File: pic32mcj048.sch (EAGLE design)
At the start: 1 part

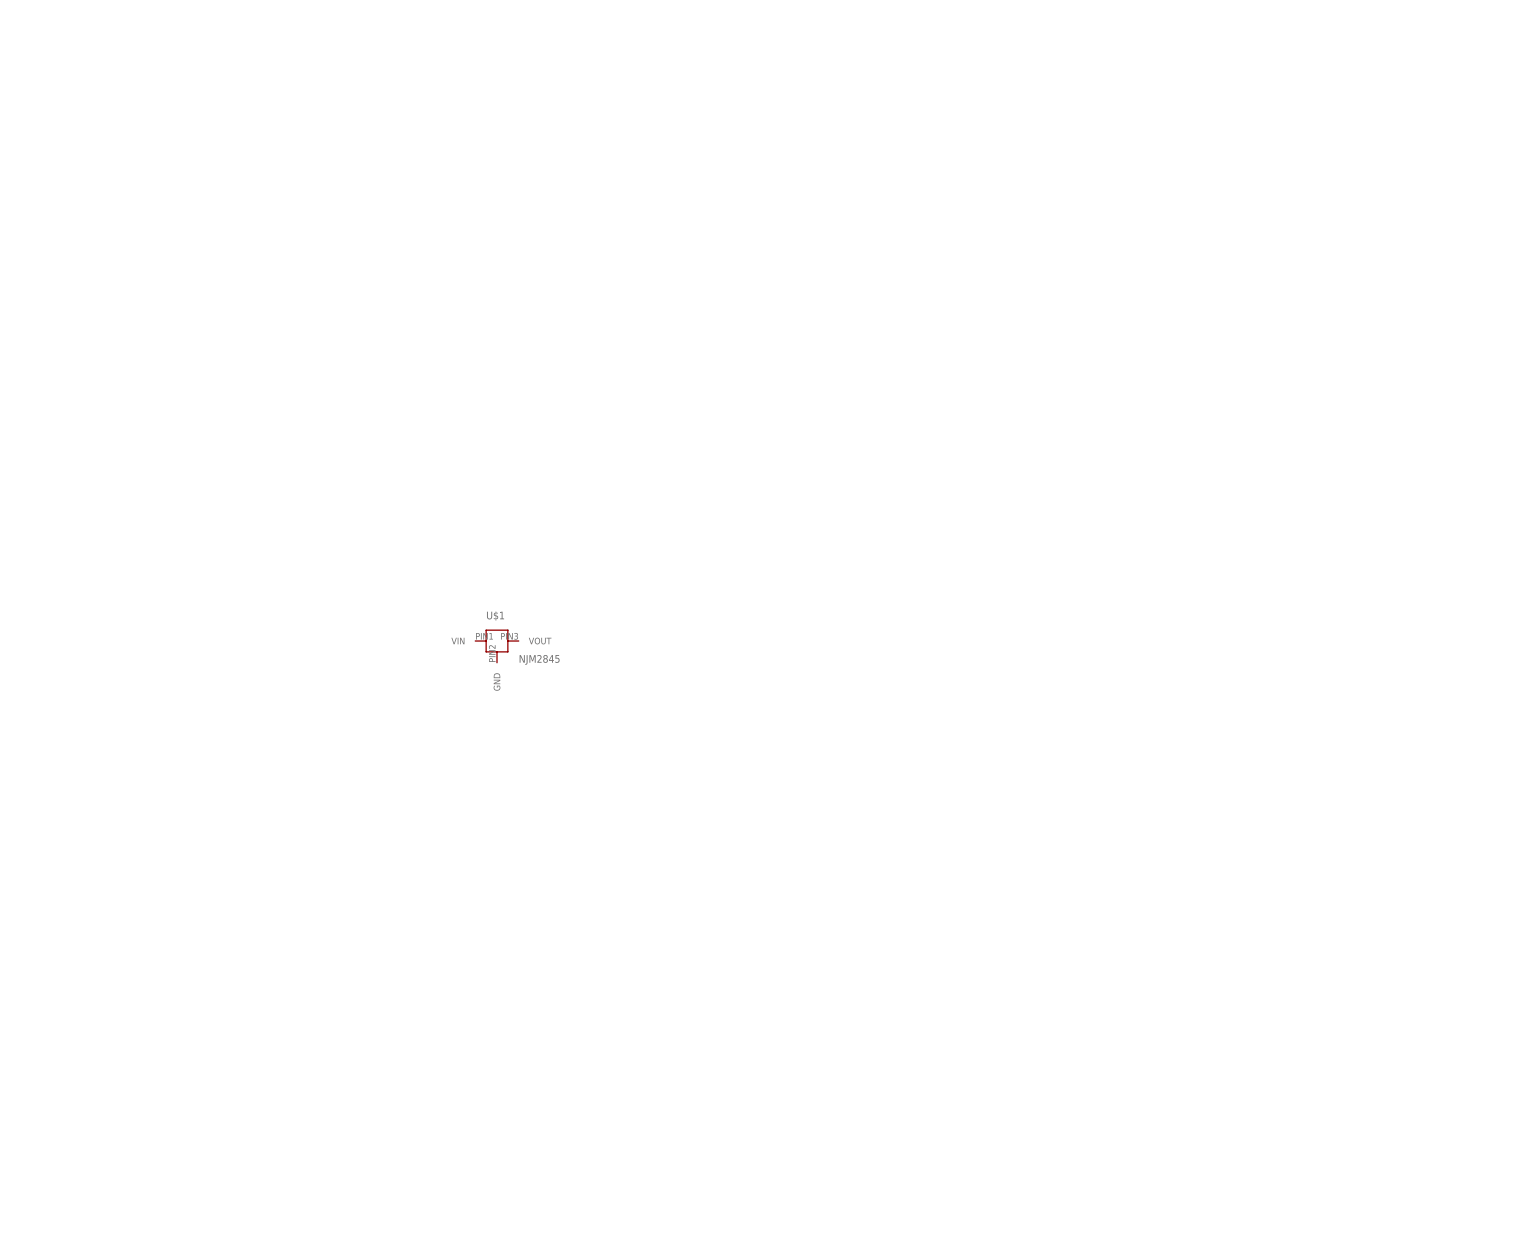
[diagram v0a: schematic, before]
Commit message: リセット回路、書き込み回路を作った
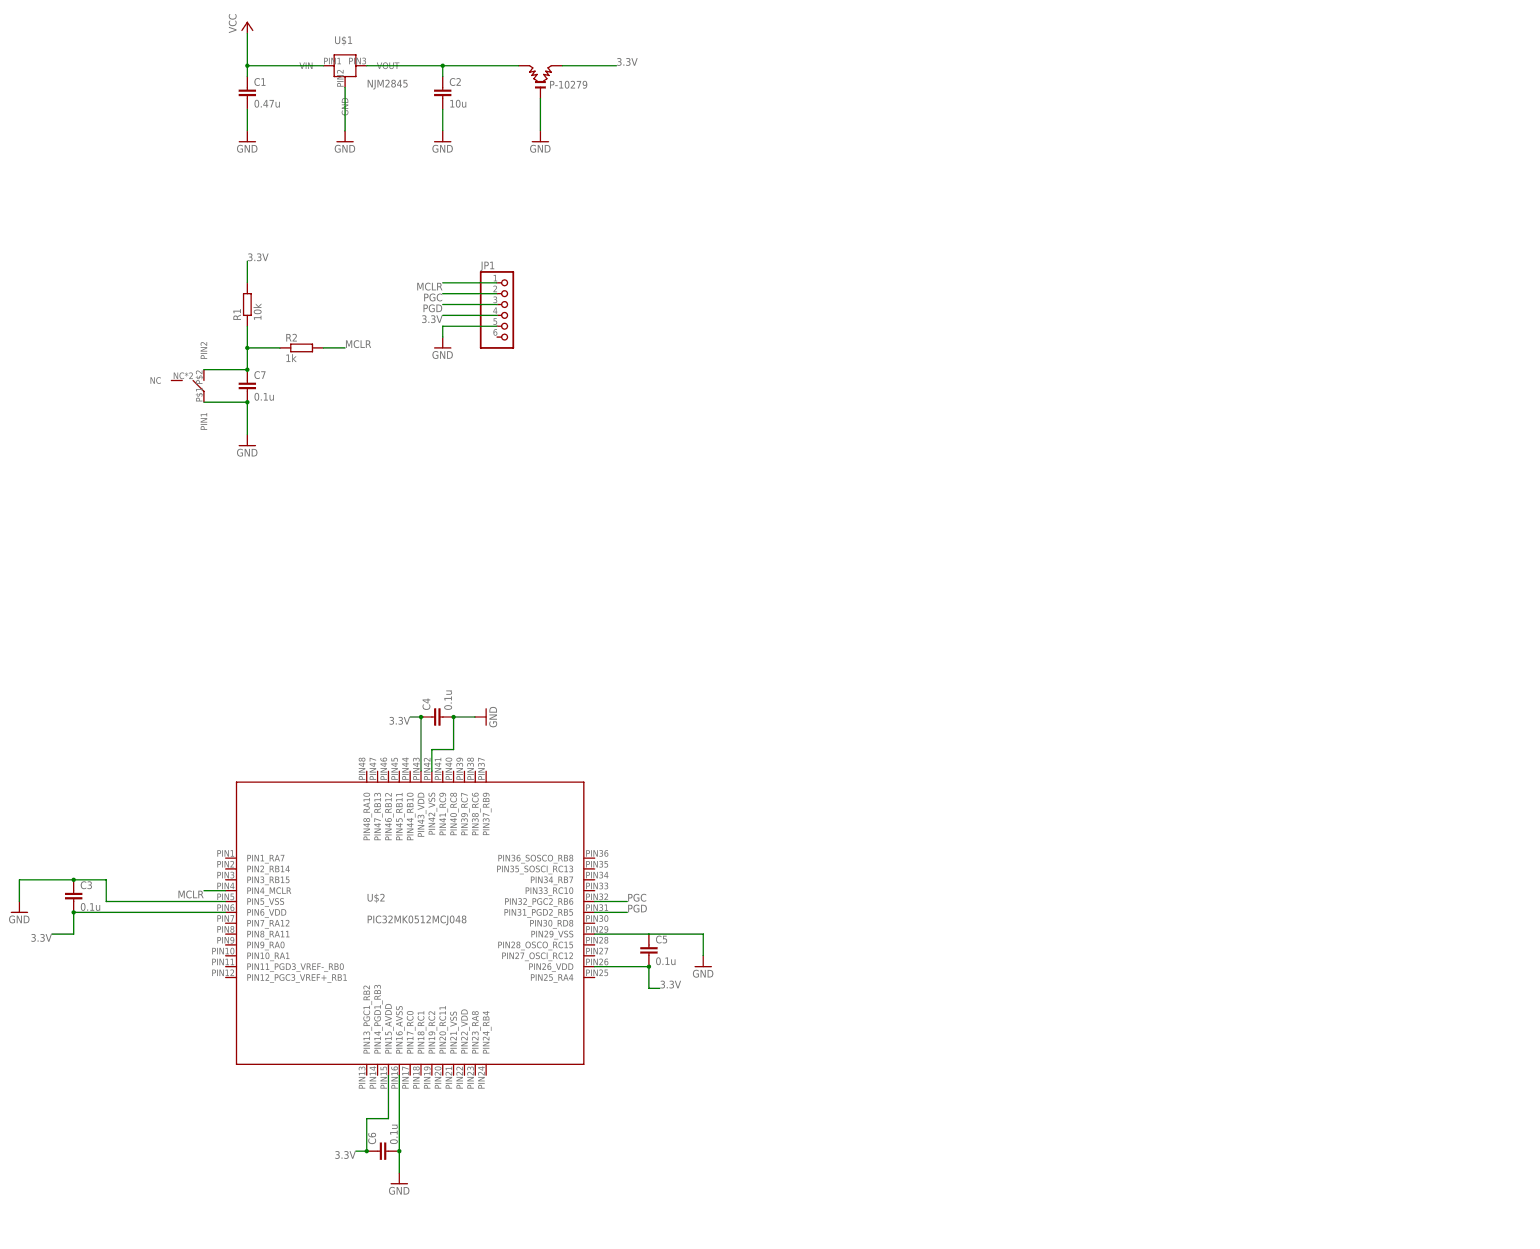
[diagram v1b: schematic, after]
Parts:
- added C1: 0.47u, rcl:C-EUC1608
- added C2: 10u, rcl:C-EUC1608
- added C3, C4, C5, C6, C7: 0.1u, rcl:C-EUC1608
- added JP1: (no value), pinhead:PINHD-1X6
- added P-10279: (no value), user_emifilter:LCL
- added R1: 10k, user_rcl:R_REG
- added R2: 1k, user_rcl:R_REG
- added U$2: PIC32MK0512MCJ048, user_ic:PIC32MK0512MCJ048
- added U$3: TAKUTOSUITTI2, user_swich:TAKUTOSUITTI2
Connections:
- new net 3.3V: C3.2, C4.1, C5.2, C6.1, JP1.4, P-10279.2, R1.2, U$2.PIN15_AVDD, U$2.PIN26_VDD, U$2.PIN43_VDD, U$2.PIN6_VDD
- new net GND: C1.2, C2.2, C3.1, C4.2, C5.1, C6.2, C7.2, JP1.5, P-10279.GND, U$1.GND, U$2.PIN16_AVSS, U$2.PIN29_VSS, U$2.PIN42_VSS, U$2.PIN5_VSS, U$3.PIN1
- new net MCLR: JP1.1, R2.2, U$2.PIN4_MCLR
- new net N$1: C2.1, P-10279.1, U$1.VOUT
- new net N$2: C7.1, R1.1, R2.1, U$3.PIN2
- new net PGC: JP1.2, U$2.PIN32_PGC2_RB6
- new net PGD: JP1.3, U$2.PIN31_PGD2_RB5
- new net VCC: C1.1, U$1.VIN
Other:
- moved on the sheet: U$1

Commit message: brdfileを編集
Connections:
- net 3.3V: now also JP1.2; no longer JP1.4
- net GND: now also JP1.3; no longer JP1.5
- net PGC: now also JP1.5; no longer JP1.2
- net PGD: now also JP1.4; no longer JP1.3
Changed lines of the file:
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@@
 <part name="R2" library="user_rcl" deviceset="R_REG" device="" value="1k"/>
 <part name="JP1" library="pinhead" library_urn="urn:adsk.eagle:library:325" deviceset="PINHD-1X6" device="" package3d_urn="urn:adsk.eagle:package:22472/2"/>
-<part name="GND10" library="supply1" library_urn="urn:adsk.eagle:library:371" deviceset="GND" device=""/>
 <part name="U$3" library="user_swich" deviceset="TAKUTOSUITTI2" device=""/>
 </parts>
@@
 <attribute name="VALUE" x="16.51" y="132.08" size="1.778" layer="96"/>
 </instance>
-<instance part="GND10" gate="1" x="7.62" y="134.62" smashed="yes">
-<attribute name="VALUE" x="5.08" y="132.08" size="1.778" layer="96"/>
-</instance>
 <instance part="U$3" gate="G$1" x="-50.8" y="124.46" smashed="yes" rot="R90"/>
 </instances>
@@
 </segment>
 <segment>
-<pinref part="JP1" gate="A" pin="4"/>
-<wire x1="20.32" y1="142.24" x2="7.62" y2="142.24" width="0.1524" layer="91"/>
-<label x="7.62" y="142.24" size="1.778" layer="95" rot="R180"/>
+<pinref part="JP1" gate="A" pin="2"/>
+<wire x1="20.32" y1="147.32" x2="7.62" y2="147.32" width="0.1524" layer="91"/>
+<label x="7.62" y="147.32" size="1.778" layer="95"/>
 </segment>
 </net>
@@
 </segment>
 <segment>
-<pinref part="JP1" gate="A" pin="5"/>
-<wire x1="20.32" y1="139.7" x2="7.62" y2="139.7" width="0.1524" layer="91"/>
-<pinref part="GND10" gate="1" pin="GND"/>
-<wire x1="7.62" y1="139.7" x2="7.62" y2="137.16" width="0.1524" layer="91"/>
+<pinref part="JP1" gate="A" pin="3"/>
+<wire x1="20.32" y1="144.78" x2="7.62" y2="144.78" width="0.1524" layer="91"/>
+<label x="7.62" y="144.78" size="1.778" layer="95"/>
 </segment>
 </net>
@@
 <pinref part="JP1" gate="A" pin="1"/>
 <wire x1="20.32" y1="149.86" x2="7.62" y2="149.86" width="0.1524" layer="91"/>
-<label x="7.62" y="149.86" size="1.778" layer="95" rot="R180"/>
+<label x="7.62" y="149.86" size="1.778" layer="95"/>
 </segment>
 </net>
@@
 </segment>
 <segment>
-<pinref part="JP1" gate="A" pin="2"/>
-<wire x1="20.32" y1="147.32" x2="7.62" y2="147.32" width="0.1524" layer="91"/>
-<label x="7.62" y="147.32" size="1.778" layer="95" rot="R180"/>
+<pinref part="JP1" gate="A" pin="5"/>
+<wire x1="20.32" y1="139.7" x2="7.62" y2="139.7" width="0.1524" layer="91"/>
+<label x="7.62" y="139.7" size="1.778" layer="95"/>
 </segment>
 </net>
@@
 </segment>
 <segment>
-<pinref part="JP1" gate="A" pin="3"/>
-<wire x1="20.32" y1="144.78" x2="7.62" y2="144.78" width="0.1524" layer="91"/>
-<label x="7.62" y="144.78" size="1.778" layer="95" rot="R180"/>
-</segment>
-</net>
+<pinref part="JP1" gate="A" pin="4"/>
+<wire x1="20.32" y1="142.24" x2="7.62" y2="142.24" width="0.1524" layer="91"/>
+<label x="7.62" y="142.24" size="1.778" layer="95"/>
+</segment>
+</net>

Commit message: sch完成
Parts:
- added C10, C11: 22p, rcl:C-EUC1608
- added C8: 0.1u, rcl:C-EUC1608
- added C9: 10u, rcl:C-EUC1608
- added IC1: (no value), user_ic:MCP2562
- added JP2, JP3: (no value), pinhead:PINHD-1X15
- added OSC1: 16M, user_osc:CSTN#
- added R3, R4, R5, R6: 10k, user_rcl:R_REG
- added R7: 1k, user_rcl:R_REG
- added R8: (no value), user_rcl:R_REG
- added R_I1: 4.7k, user_rcl:R_SHUGOU2
- added U$5: RGB_LED, user_leds:RGB_LED
- added U$6: FDC6305, user_tr_fet_igbt:FDC6305
- added U$7: NJM2380, user_ic:NJM2380
- added X1: 32.768k, user_osc:FC255
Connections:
- new net C1RX: IC1.RXD, U$2.PIN25_RA4
- new net C1TX: IC1.TXD, U$2.PIN34_RB7
- new net CANH: IC1.CANH, JP3.9
- new net CANL: IC1.CANL, JP3.10
- new net LED_G: U$2.PIN33_RC10, U$6.PIN1_G1
- new net LED_R: U$2.PIN30_RD8, U$6.PIN3_G2
- new net N$11: R8.1, U$2.PIN36_SOSCO_RB8
- new net N$13: R4.1, U$5.B_A
- new net N$14: R5.1, U$5.G_A
- new net N$15: R6.1, U$5.R_A
- new net N$21: R_I1.7, R_I1.8, U$7.PIN5_REF
- new net N$3: OSC1.IN, U$2.PIN28_OSCO_RC15
- new net N$4: OSC1.OUT, U$2.PIN27_OSCI_RC12
- new net N$45: R_I1.2, R_I1.3
- new net N$46: R_I1.5, R_I1.6
- new net N$5: IC1.STBY, R3.1
- new net N$6: C10.1, R8.2, X1.2
- new net N$7: C11.1, U$2.PIN35_SOSCI_RC13, X1.1
- new net N$8: U$5.G_K, U$6.PIN6_D1
- new net N$9: U$5.R_K, U$6.PIN4_D2
- new net RA0: U$2.PIN9_RA0
- new net RA1: U$2.PIN10_RA1
- new net RA10: JP2.10, U$2.PIN48_RA10
- new net RA11: U$2.PIN8_RA11
- new net RA12: U$2.PIN7_RA12
- new net RA7: U$2.PIN1_RA7
- new net RA8: JP3.2, U$2.PIN23_RA8
- new net RB10: JP2.6, U$2.PIN44_RB10
- new net RB11: JP2.7, U$2.PIN45_RB11
- new net RB12: JP2.8, U$2.PIN46_RB12
- new net RB13: JP2.9, U$2.PIN47_RB13
- new net RB14: U$2.PIN2_RB14
- new net RB15: U$2.PIN3_RB15
- new net RB2: JP3.8, U$2.PIN13_PGC1_RB2
- new net RB3: JP3.7, U$2.PIN14_PGD1_RB3
- new net RB4: JP3.1, U$2.PIN24_RB4
- new net RB9: JP2.1, U$2.PIN37_RB9
- new net RC0: JP3.6, U$2.PIN17_RC0
- new net RC1: JP3.5, U$2.PIN18_RC1
- new net RC11: JP3.3, U$2.PIN20_RC11
- new net RC2: JP3.4, U$2.PIN19_RC2
- new net RC6: JP2.2, U$2.PIN38_RC6
- new net RC7: JP2.3, U$2.PIN39_RC7
- new net RC8: JP2.4, U$2.PIN40_RC8
- new net RC9: JP2.5, U$2.PIN41_RC9
- new net VREF+: C9.1, R7.1, R_I1.1, U$2.PIN12_PGC3_VREF+_RB1, U$7.PIN4_C
- net 3.3V: now also C8.2, IC1.VIO, JP2.11, JP3.11, R4.2, R5.2, R6.2, U$2.PIN22_VDD
- net GND: now also C10.2, C11.2, C8.1, C9.2, IC1.VSS, JP2.12, JP2.14, JP3.12, JP3.14, OSC1.GND, R_I1.4, U$2.PIN11_PGD3_VREF-_RB0, U$2.PIN21_VSS, U$5.B_K, U$6.PIN2_S2, U$6.PIN5_S1, U$7.PIN2_A
- net VCC: now also IC1.VDD, JP2.13, JP2.15, JP3.13, JP3.15, R3.2, R7.2
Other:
- moved on the sheet: C1, C2, C3, C4, C5, C6, C7, JP1, P-10279, R1, R2, U$1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

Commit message: 基本設計完了、あとは調整など
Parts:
- added C12, C13: 0.1u, rcl:C-EUC1608
- added C14: 0.47u, rcl:C-EUC1608
- added R9: 120, user_rcl:R_REG
- added U$4: XH_2P, user_conector:XH_2P
- added U$8: NJM2391, user_ic:NJM2391
- R4, R5, R6: value 10k -> 1k
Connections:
- removed net CANH: IC1.CANH, JP3.9
- removed net CANL: IC1.CANL, JP3.10
- new net +5V: C1.1, C12.1, C13.1, IC1.VDD, JP3.15, R3.2, R7.2, U$1.VIN, U$8.VOUT
- new net CAN_N: IC1.CANL, JP3.1, R9.1
- new net CAN_P: IC1.CANH, JP3.2, R9.2
- net 3.3V: now also JP2.14; no longer JP2.11, JP3.11
- net GND: now also C12.2, C13.2, C14.2, JP2.15, U$4.PIN1, U$8.GND; no longer JP2.12, JP2.14, JP3.12, JP3.14
- net RA0: now also JP3.12
- net RA1: now also JP3.11
- net RA11: now also JP3.13
- net RA12: now also JP3.14
- net RA7: now also JP2.11
- net RA8: now also JP3.4; no longer JP3.2
- net RB14: now also JP2.12
- net RB15: now also JP2.13
- net RB2: now also JP3.10; no longer JP3.8
- net RB3: now also JP3.9; no longer JP3.7
- net RB4: now also JP3.3; no longer JP3.1
- net RC0: now also JP3.8; no longer JP3.6
- net RC1: now also JP3.7; no longer JP3.5
- net RC11: now also JP3.5; no longer JP3.3
- net RC2: now also JP3.6; no longer JP3.4
- net VCC: now also C14.1, U$4.PIN2, U$8.VIN; no longer C1.1, IC1.VDD, JP2.13, JP2.15, JP3.13, JP3.15, R3.2, R7.2, U$1.VIN

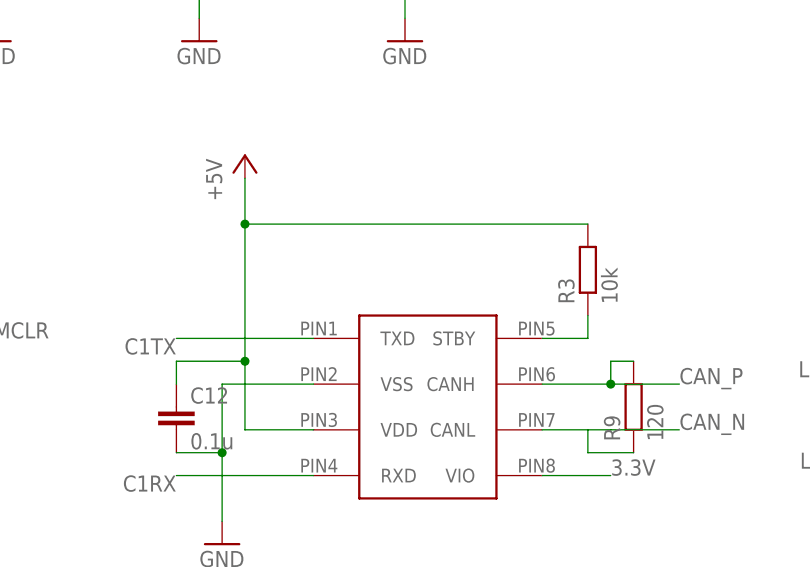
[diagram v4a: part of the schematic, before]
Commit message: mcp2562スタンバイピンプルダウン
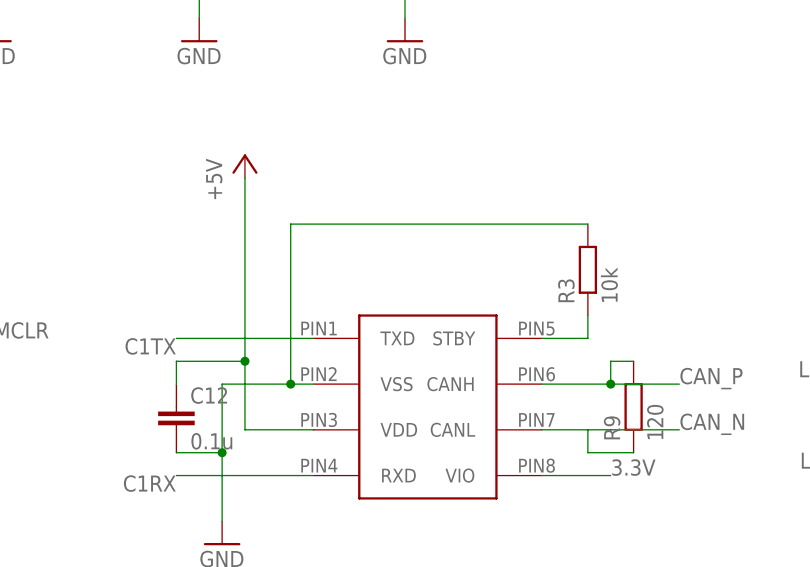
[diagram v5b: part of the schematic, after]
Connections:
- net +5V: no longer R3.2
- net GND: now also R3.2
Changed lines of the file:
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@@
 </segment>
 <segment>
-<wire x1="20.32" y1="104.14" x2="10.16" y2="104.14" width="0.1524" layer="91"/>
+<wire x1="20.32" y1="104.14" x2="17.78" y2="104.14" width="0.1524" layer="91"/>
+<wire x1="17.78" y1="104.14" x2="10.16" y2="104.14" width="0.1524" layer="91"/>
 <wire x1="10.16" y1="104.14" x2="10.16" y2="96.52" width="0.1524" layer="91"/>
 <pinref part="GND10" gate="1" pin="GND"/>
@@
 <wire x1="5.08" y1="96.52" x2="10.16" y2="96.52" width="0.1524" layer="91"/>
 <junction x="10.16" y="96.52"/>
+<wire x1="17.78" y1="104.14" x2="17.78" y2="121.92" width="0.1524" layer="91"/>
+<wire x1="17.78" y1="121.92" x2="50.8" y2="121.92" width="0.1524" layer="91"/>
+<junction x="17.78" y="104.14"/>
+<pinref part="R3" gate="G$1" pin="2"/>
 </segment>
 <segment>
@@
 <wire x1="20.32" y1="99.06" x2="12.7" y2="99.06" width="0.1524" layer="91"/>
 <wire x1="12.7" y1="99.06" x2="12.7" y2="106.68" width="0.1524" layer="91"/>
-<pinref part="R3" gate="G$1" pin="2"/>
-<wire x1="12.7" y1="106.68" x2="12.7" y2="121.92" width="0.1524" layer="91"/>
-<wire x1="12.7" y1="121.92" x2="50.8" y2="121.92" width="0.1524" layer="91"/>
+<wire x1="12.7" y1="106.68" x2="12.7" y2="127" width="0.1524" layer="91"/>
 <pinref part="IC1" gate="G$1" pin="VDD"/>
 <pinref part="C12" gate="G$1" pin="1"/>
@@
 <junction x="12.7" y="106.68"/>
 <pinref part="P+2" gate="1" pin="+5V"/>
-<wire x1="12.7" y1="127" x2="12.7" y2="121.92" width="0.1524" layer="91"/>
-<junction x="12.7" y="121.92"/>
-</segment>
-</net>
+</segment>
+</net>
